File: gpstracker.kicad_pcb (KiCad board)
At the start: 2 copper layers, 75.2 x 54.6 mm, 80 parts, among them IC1 SIM808, J1 Molex 47346-0001, J2 Leds, J3 47553-0001, J4 CONN_COAXIAL, J5 CONN_COAXIAL, J6 Micro_SD_Card, Q1 DMP1045U, SW1 Reset, U1 MCP73832-5-OT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

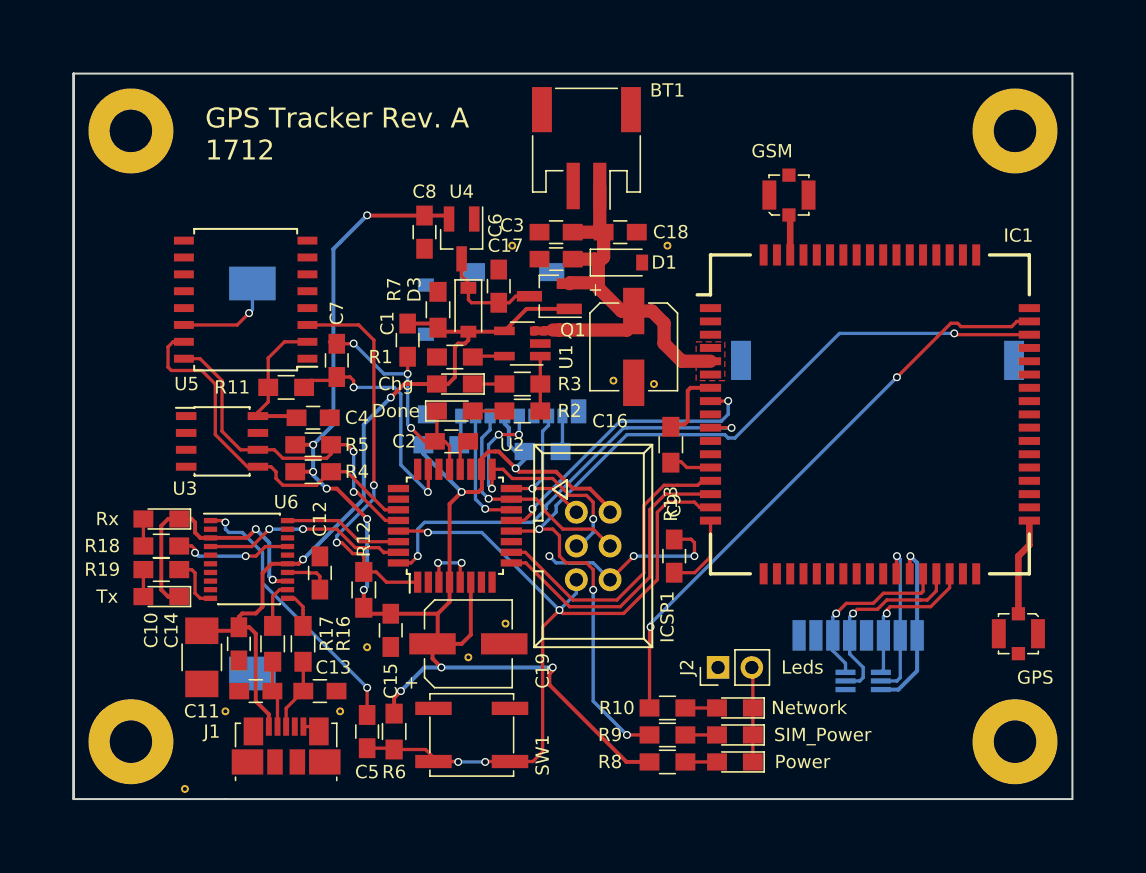
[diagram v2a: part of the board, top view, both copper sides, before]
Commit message: Added vias to the whole PCB
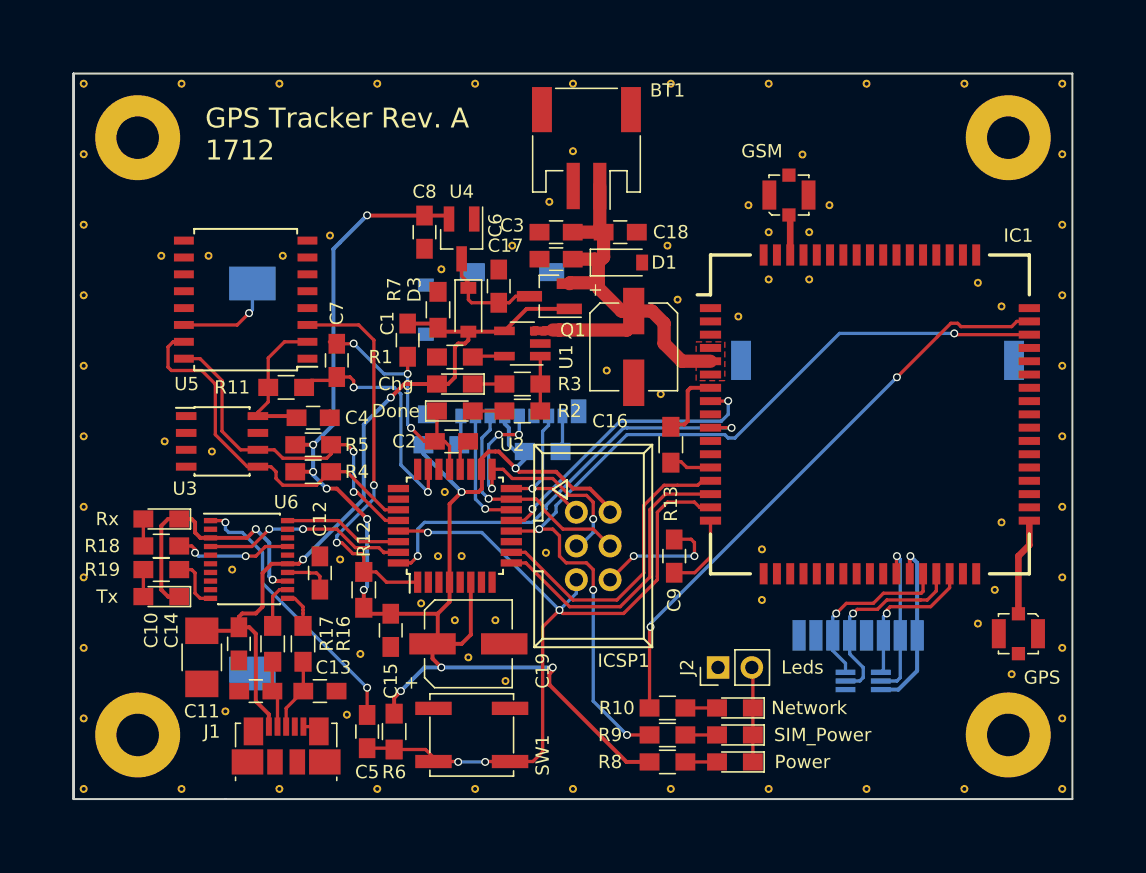
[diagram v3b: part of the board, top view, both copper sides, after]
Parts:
- added VIA**: Via-0.6mm, custom-conn:Via-0.6mm, F.Cu at (133.3, 114.3)
- added VIA**: Via-0.6mm, custom-conn:Via-0.6mm, F.Cu at (128.8, 100.1)
- added VIA**: Via-0.6mm, custom-conn:Via-0.6mm, F.Cu at (127.0, 108.5)
- added VIA**: Via-0.6mm, custom-conn:Via-0.6mm, F.Cu at (129.5, 109.7)
- added VIA**: Via-0.6mm, custom-conn:Via-0.6mm, F.Cu at (128.5, 83.3)
- added VIA**: Via-0.6mm, custom-conn:Via-0.6mm, F.Cu at (116.6, 82.3)
- added VIA**: Via-0.6mm, custom-conn:Via-0.6mm, F.Cu at (111.0, 82.3)
- added VIA**: Via-0.6mm, custom-conn:Via-0.6mm, F.Cu at (107.7, 96.3)
- added VIA**: Via-0.6mm, custom-conn:Via-0.6mm, F.Cu at (120.9, 105.2)
- added VIA**: Via-0.6mm, custom-conn:Via-0.6mm, F.Cu at (112.8, 105.9)
- added VIA**: Via-0.6mm, custom-conn:Via-0.6mm, F.Cu at (150.9, 86.9)
- added VIA**: Via-0.6mm, custom-conn:Via-0.6mm, F.Cu at (138.4, 74.4)
- added VIA**: Via-0.6mm, custom-conn:Via-0.6mm, F.Cu at (146.3, 85.6)
- added VIA**: Via-0.6mm, custom-conn:Via-0.6mm, F.Cu at (152.7, 104.4)
- added VIA**: Via-0.6mm, custom-conn:Via-0.6mm, F.Cu at (152.7, 108.2)
- added VIA**: Via-0.6mm, custom-conn:Via-0.6mm, F.Cu at (153.2, 84.1)
- added VIA**: Via-0.6mm, custom-conn:Via-0.6mm, F.Cu at (156.2, 84.1)
- added VIA**: Via-0.6mm, custom-conn:Via-0.6mm, F.Cu at (168.9, 84.3)
- added VIA**: Via-0.6mm, custom-conn:Via-0.6mm, F.Cu at (170.7, 86.1)
- added VIA**: Via-0.6mm, custom-conn:Via-0.6mm, F.Cu at (170.7, 102.4)
- added VIA**: Via-0.6mm, custom-conn:Via-0.6mm, F.Cu at (170.2, 107.4)
- added VIA**: Via-0.6mm, custom-conn:Via-0.6mm, F.Cu at (171.4, 113.8)
- added VIA**: Via-0.6mm, custom-conn:Via-0.6mm, F.Cu at (136.7, 78.2)
- added VIA**: Via-0.6mm, custom-conn:Via-0.6mm, F.Cu at (153.2, 80.5)
- added VIA**: Via-0.6mm, custom-conn:Via-0.6mm, F.Cu at (156.2, 80.5)
- added VIA**: Via-0.6mm, custom-conn:Via-0.6mm, F.Cu at (155.7, 74.7)
- added VIA**: Via-0.6mm, custom-conn:Via-0.6mm, F.Cu at (157.7, 78.5)
- added VIA**: Via-0.6mm, custom-conn:Via-0.6mm, F.Cu at (151.6, 78.5)
- added VIA**: Via-0.6mm, custom-conn:Via-0.6mm, F.Cu at (168.9, 110.0)
- added VIA**: Via-0.6mm, custom-conn:Via-0.6mm, F.Cu at (175.3, 117.1)
- added VIA**: Via-0.6mm, custom-conn:Via-0.6mm, F.Cu at (175.3, 111.8)
- added VIA**: Via-0.6mm, custom-conn:Via-0.6mm, F.Cu at (175.3, 106.5)
- added VIA**: Via-0.6mm, custom-conn:Via-0.6mm, F.Cu at (175.3, 101.2)
- added VIA**: Via-0.6mm, custom-conn:Via-0.6mm, F.Cu at (130.0, 104.9)
- added VIA**: Via-0.6mm, custom-conn:Via-0.6mm, F.Cu at (175.3, 95.9)
- added VIA**: Via-0.6mm, custom-conn:Via-0.6mm, F.Cu at (175.3, 90.6)
- added VIA**: Via-0.6mm, custom-conn:Via-0.6mm, F.Cu at (175.3, 85.3)
- added VIA**: Via-0.6mm, custom-conn:Via-0.6mm, F.Cu at (175.3, 80.0)
- added VIA**: Via-0.6mm, custom-conn:Via-0.6mm, F.Cu at (175.3, 74.7)
- added VIA**: Via-0.6mm, custom-conn:Via-0.6mm, F.Cu at (175.3, 69.3)
- added VIA**: Via-0.6mm, custom-conn:Via-0.6mm, F.Cu at (167.9, 69.3)
- added VIA**: Via-0.6mm, custom-conn:Via-0.6mm, F.Cu at (160.5, 69.3)
- added VIA**: Via-0.6mm, custom-conn:Via-0.6mm, F.Cu at (153.2, 69.3)
- added VIA**: Via-0.6mm, custom-conn:Via-0.6mm, F.Cu at (145.8, 69.3)
- added VIA**: Via-0.6mm, custom-conn:Via-0.6mm, F.Cu at (128.3, 104.9)
- added VIA**: Via-0.6mm, custom-conn:Via-0.6mm, F.Cu at (138.4, 69.3)
- added VIA**: Via-0.6mm, custom-conn:Via-0.6mm, F.Cu at (131.1, 69.3)
- added VIA**: Via-0.6mm, custom-conn:Via-0.6mm, F.Cu at (123.7, 69.3)
- added VIA**: Via-0.6mm, custom-conn:Via-0.6mm, F.Cu at (116.3, 69.3)
- added VIA**: Via-0.6mm, custom-conn:Via-0.6mm, F.Cu at (109.0, 69.3)
- added VIA**: Via-0.6mm, custom-conn:Via-0.6mm, F.Cu at (101.6, 69.3)
- added VIA**: Via-0.6mm, custom-conn:Via-0.6mm, F.Cu at (101.6, 74.7)
- added VIA**: Via-0.6mm, custom-conn:Via-0.6mm, F.Cu at (101.6, 80.0)
- added VIA**: Via-0.6mm, custom-conn:Via-0.6mm, F.Cu at (101.6, 85.3)
- added VIA**: Via-0.6mm, custom-conn:Via-0.6mm, F.Cu at (101.6, 90.6)
- added VIA**: Via-0.6mm, custom-conn:Via-0.6mm, F.Cu at (136.4, 104.6)
- added VIA**: Via-0.6mm, custom-conn:Via-0.6mm, F.Cu at (101.6, 95.9)
- added VIA**: Via-0.6mm, custom-conn:Via-0.6mm, F.Cu at (101.6, 101.2)
- added VIA**: Via-0.6mm, custom-conn:Via-0.6mm, F.Cu at (101.6, 106.5)
- added VIA**: Via-0.6mm, custom-conn:Via-0.6mm, F.Cu at (101.6, 111.8)
- added VIA**: Via-0.6mm, custom-conn:Via-0.6mm, F.Cu at (101.6, 117.1)
- added VIA**: Via-0.6mm, custom-conn:Via-0.6mm, F.Cu at (175.3, 122.4)
- added VIA**: Via-0.6mm, custom-conn:Via-0.6mm, F.Cu at (167.9, 122.4)
- added VIA**: Via-0.6mm, custom-conn:Via-0.6mm, F.Cu at (160.5, 122.4)
- added VIA**: Via-0.6mm, custom-conn:Via-0.6mm, F.Cu at (153.2, 122.4)
- added VIA**: Via-0.6mm, custom-conn:Via-0.6mm, F.Cu at (145.8, 122.4)
- added VIA**: Via-0.6mm, custom-conn:Via-0.6mm, F.Cu at (107.4, 82.3)
- added VIA**: Via-0.6mm, custom-conn:Via-0.6mm, F.Cu at (138.4, 122.4)
- added VIA**: Via-0.6mm, custom-conn:Via-0.6mm, F.Cu at (131.1, 122.4)
- added VIA**: Via-0.6mm, custom-conn:Via-0.6mm, F.Cu at (123.7, 122.4)
- added VIA**: Via-0.6mm, custom-conn:Via-0.6mm, F.Cu at (116.3, 122.4)
- added VIA**: Via-0.6mm, custom-conn:Via-0.6mm, F.Cu at (109.0, 122.4)
- added VIA**: Via-0.6mm, custom-conn:Via-0.6mm, F.Cu at (120.1, 80.8)
- added VIA**: Via-0.6mm, custom-conn:Via-0.6mm, F.Cu at (111.3, 97.0)
- moved VIA** 7.62 mm to (101.6, 122.4)
- moved VIA** 0.92 mm to (141.0, 90.9)
- moved VIA** 0.92 mm to (145.0, 92.7)
- moved VIA** 0.80 mm to (132.6, 109.7)
- moved REF** 0.72 mm to (171.2, 73.4)
- moved REF** 0.72 mm to (171.2, 118.4)
- moved REF** 0.72 mm to (105.7, 73.4)
- moved VIA** 0.72 mm to (122.4, 112.3)
- moved REF** 0.72 mm to (105.7, 118.4)
- moved VIA** 0.57 mm to (121.4, 116.8)
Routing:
- net GND: track 53.9 -> 43.8 mm, vias 9 -> 6

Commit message: Antennas tracks impedance to 50ohm (1.5mm thick)
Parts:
- removed the VIA** at (136.4, 104.6)
- moved J5 0.13 mm to (154.8, 77.7)
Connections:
- J3 pad GND1: (no net) -> GND
- J3 pad GND2: (no net) -> GND
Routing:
- net GND: track 43.8 -> 49.9 mm, vias 6 -> 7
- net /GSM: track 3.05 -> 1.40 mm
- added copper zone on F.Cu, net /GSM
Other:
- net class RF: trace_width 0.5 -> 1.5

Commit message: Submitted version for verification
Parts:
- added VIA**: Via-0.6mm, custom-conn:Via-0.6mm, F.Cu at (116.1, 95.5)
- added VIA**: Via-0.6mm, custom-conn:Via-0.6mm, F.Cu at (153.2, 97.0)
- added VIA**: Via-0.6mm, custom-conn:Via-0.6mm, F.Cu at (165.9, 93.0)
- added VIA**: Via-0.6mm, custom-conn:Via-0.6mm, F.Cu at (160.5, 99.8)
- added VIA**: Via-0.6mm, custom-conn:Via-0.6mm, F.Cu at (158.0, 78.6)
- added VIA**: Via-0.6mm, custom-conn:Via-0.6mm, F.Cu at (151.6, 78.6)
- added VIA**: Via-0.6mm, custom-conn:Via-0.6mm, F.Cu at (175.0, 109.7)
- added VIA**: Via-0.6mm, custom-conn:Via-0.6mm, F.Cu at (173.9, 105.8)
- added VIA**: Via-0.6mm, custom-conn:Via-0.6mm, F.Cu at (170.3, 105.5)
- added VIA**: Via-0.6mm, custom-conn:Via-0.6mm, F.Cu at (168.9, 109.6)
- added VIA**: Via-0.6mm, custom-conn:Via-0.6mm, F.Cu at (170.6, 103.6)
- added VIA**: Via-0.6mm, custom-conn:Via-0.6mm, F.Cu at (126.7, 110.0)
- added VIA**: Via-0.6mm, custom-conn:Via-0.6mm, F.Cu at (174.5, 103.9)
- added VIA**: Via-0.6mm, custom-conn:Via-0.6mm, F.Cu at (174.0, 108.1)
- added VIA**: Via-0.6mm, custom-conn:Via-0.6mm, F.Cu at (174.5, 113.3)
- added VIA**: Via-0.6mm, custom-conn:Via-0.6mm, F.Cu at (169.5, 113.3)
- added VIA**: Via-0.6mm, custom-conn:Via-0.6mm, F.Cu at (168.8, 103.9)
- added VIA**: Via-0.6mm, custom-conn:Via-0.6mm, F.Cu at (154.8, 74.5)
- added VIA**: Via-0.6mm, custom-conn:Via-0.6mm, F.Cu at (152.9, 75.4)
- added VIA**: Via-0.6mm, custom-conn:Via-0.6mm, F.Cu at (154.9, 102.6)
- added VIA**: Via-0.6mm, custom-conn:Via-0.6mm, F.Cu at (169.4, 91.2)
- added VIA**: Via-0.6mm, custom-conn:Via-0.6mm, F.Cu at (153.2, 91.2)
- added VIA**: Via-0.6mm, custom-conn:Via-0.6mm, F.Cu at (154.7, 88.4)
- added VIA**: Via-0.6mm, custom-conn:Via-0.6mm, F.Cu at (161.3, 85.9)
- added VIA**: Via-0.6mm, custom-conn:Via-0.6mm, F.Cu at (167.4, 98.6)
- added VIA**: Via-0.6mm, custom-conn:Via-0.6mm, F.Cu at (159.5, 90.2)
- moved VIA** 1.78 mm to (168.9, 111.8)
- moved VIA** 1.55 mm to (158.0, 77.0)
- moved VIA** 1.52 mm to (151.6, 77.0)
- moved VIA** 1.27 mm to (156.7, 75.4)
- moved VIA** 1.15 mm to (170.6, 101.2)
- moved VIA** 0.72 mm to (156.7, 80.0)
- moved VIA** 0.63 mm to (138.4, 73.8)
- moved VIA** 0.57 mm to (152.9, 80.0)
- moved VIA** 0.52 mm to (172.0, 113.9)
- moved VIA** 0.40 mm to (170.1, 107.8)

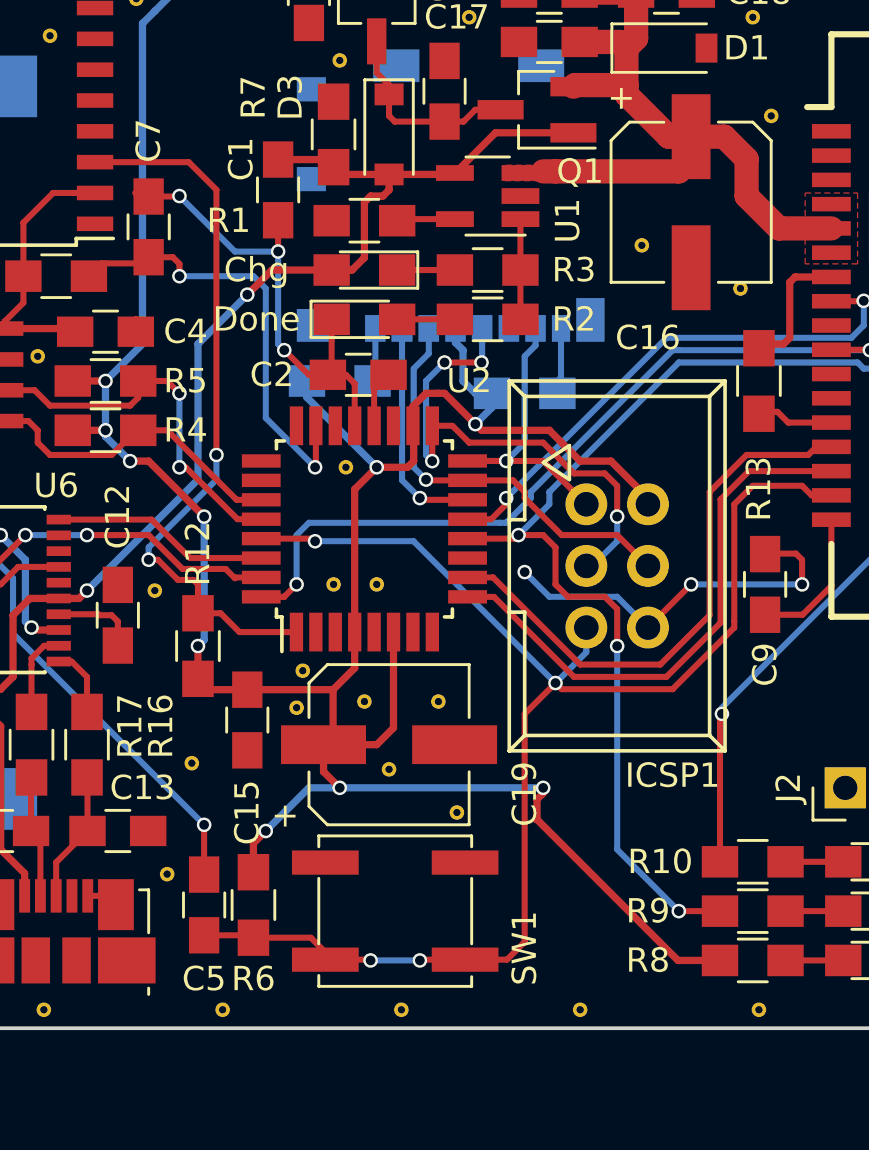
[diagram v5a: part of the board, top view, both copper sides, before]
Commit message: Change a few tracks/via to avoid ground planes breaks
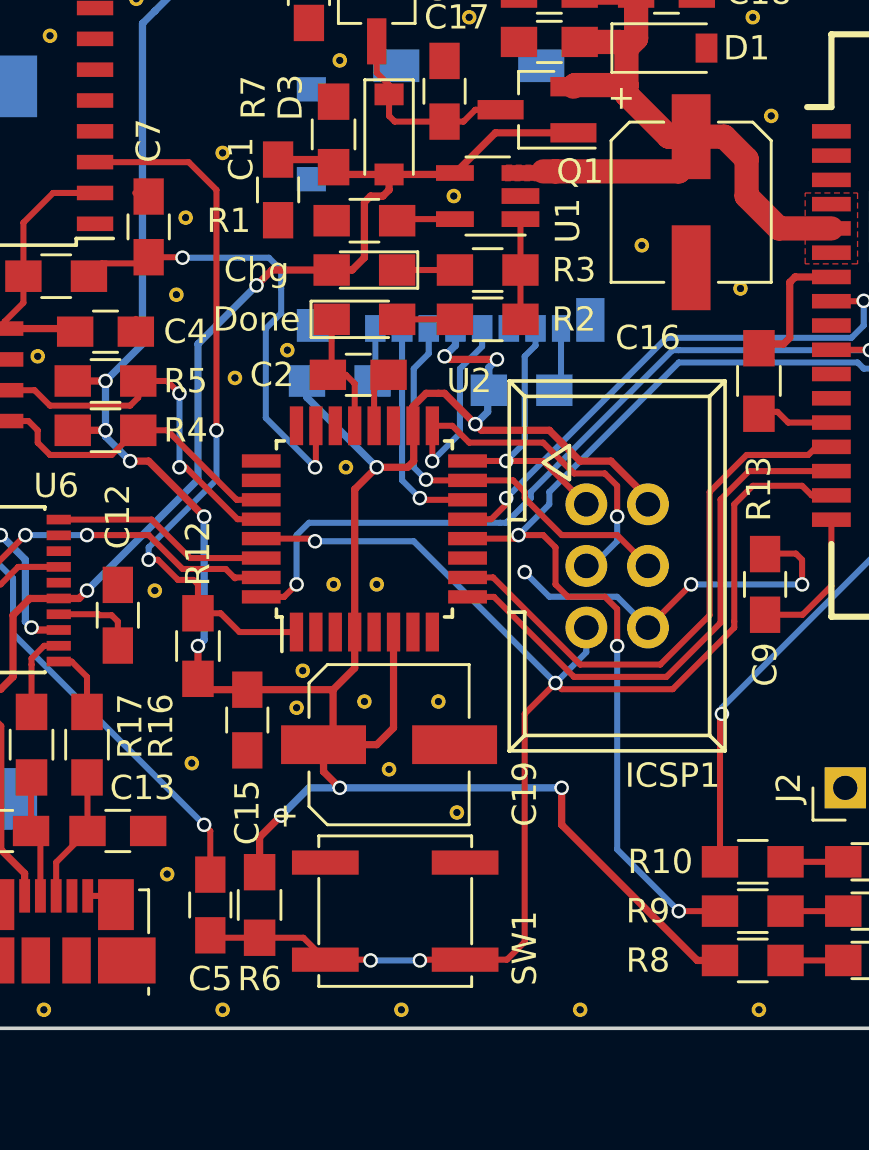
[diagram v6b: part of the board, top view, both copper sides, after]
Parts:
- added VIA**: Via-0.6mm, custom-conn:Via-0.6mm, F.Cu at (133.2, 88.9)
- added VIA**: Via-0.6mm, custom-conn:Via-0.6mm, F.Cu at (121.8, 93.0)
- added VIA**: Via-0.6mm, custom-conn:Via-0.6mm, F.Cu at (124.2, 96.4)
- added VIA**: Via-0.6mm, custom-conn:Via-0.6mm, F.Cu at (123.7, 87.1)
- added VIA**: Via-0.6mm, custom-conn:Via-0.6mm, F.Cu at (122.2, 89.8)
- added VIA**: Via-0.6mm, custom-conn:Via-0.6mm, F.Cu at (126.4, 95.2)
- moved C5 0.25 mm to (123.2, 118.1)
- moved R6 0.25 mm to (125.2, 118.1)
- moved R14 0.18 mm to (136.0, 96.9)
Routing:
- net GND: track 49.9 -> 35.9 mm, vias 7 -> 4
- net +3V3: track 121.3 -> 123.8 mm, vias 11 -> 13
- net /ARD_SCK: track 21.5 -> 20.4 mm, vias 4 -> 2
- net /RTC_PWR: track 18.3 -> 19.3 mm

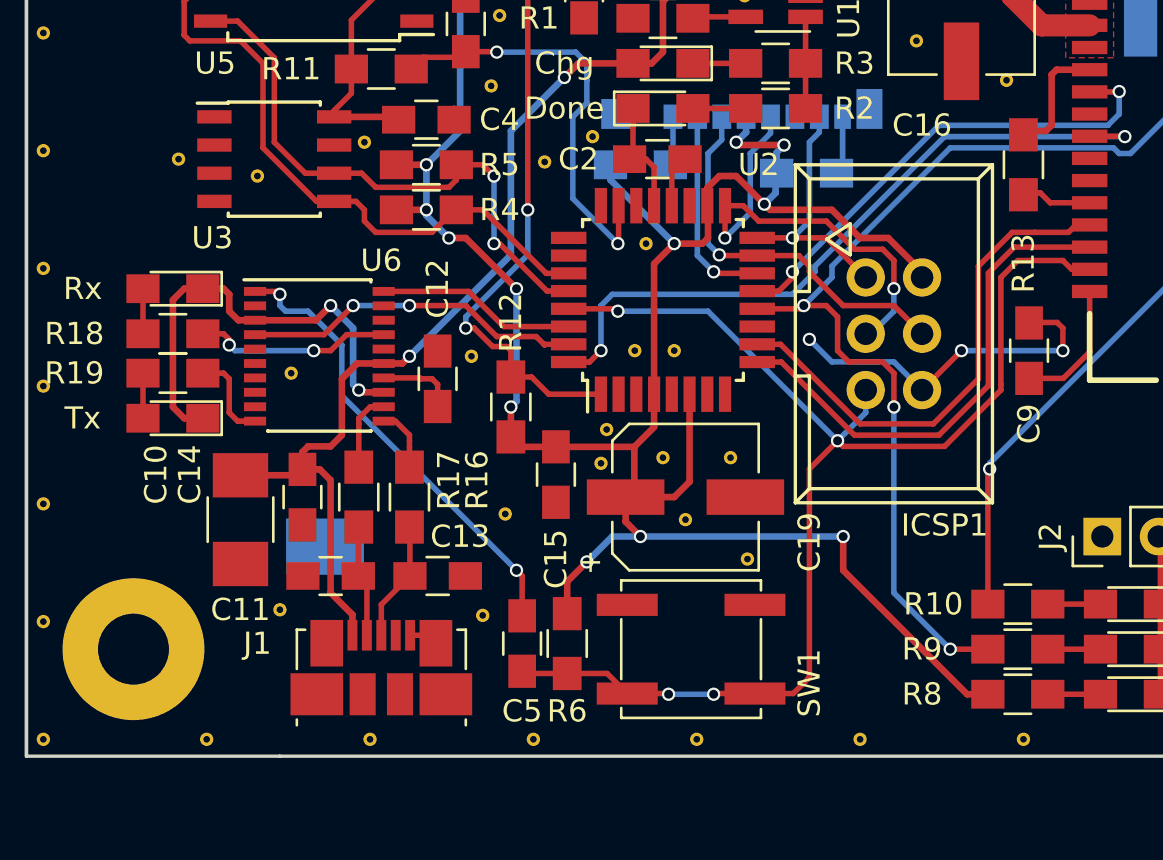
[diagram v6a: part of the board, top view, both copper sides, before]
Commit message: Made the usb connector vertical
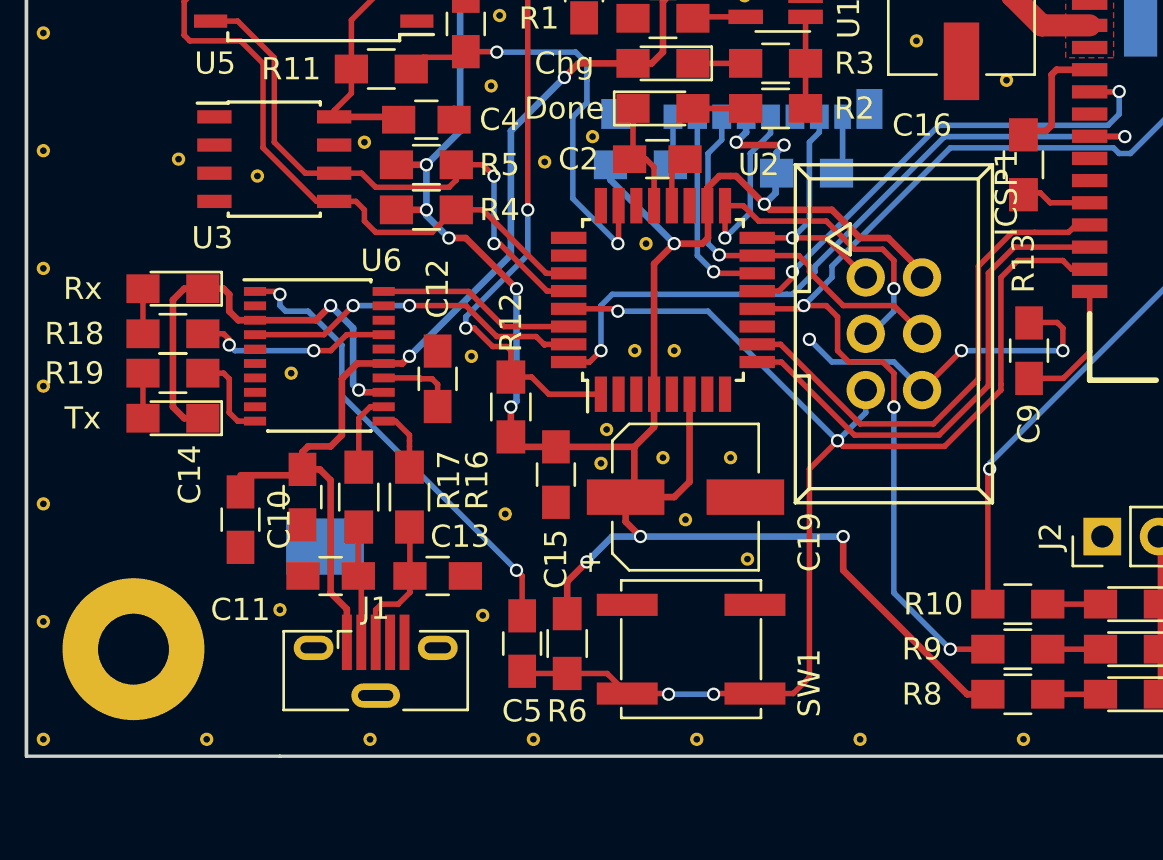
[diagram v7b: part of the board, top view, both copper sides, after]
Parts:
- C10: footprint Capacitors_SMD:C_1210_HandSoldering -> Capacitors_SMD:C_0805_HandSoldering
- C9: value 10uF -> 4.7uF
- J1: value Molex 47346-0001 -> Molex 105133-0002; footprint Connectors_USB:USB_Micro-B_Molex_47346-0001 -> custom-conn:USB_Micro-B_Vertical_Molex-105133-0001_HandSoldering
- moved J1 1.05 mm to (116.6, 119.4)
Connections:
- J3 pad GND1: GND -> (no net)
- J3 pad GND2: GND -> (no net)
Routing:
- net GND: track 35.9 -> 34.6 mm
- net Net-(C13-Pad1): track 5.42 -> 6.29 mm
